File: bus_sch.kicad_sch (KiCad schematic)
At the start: 12 parts, among them J2 Conn_01x01_Female, J3 Conn_01x01_Female, J4 Conn_02x20_Odd_Even, J5 Conn_01x01_Female, J6 Conn_01x01_Female, J7 Conn_01x01_Female, J8 Conn_01x01_Female, J9 Conn_02x10_Odd_Even

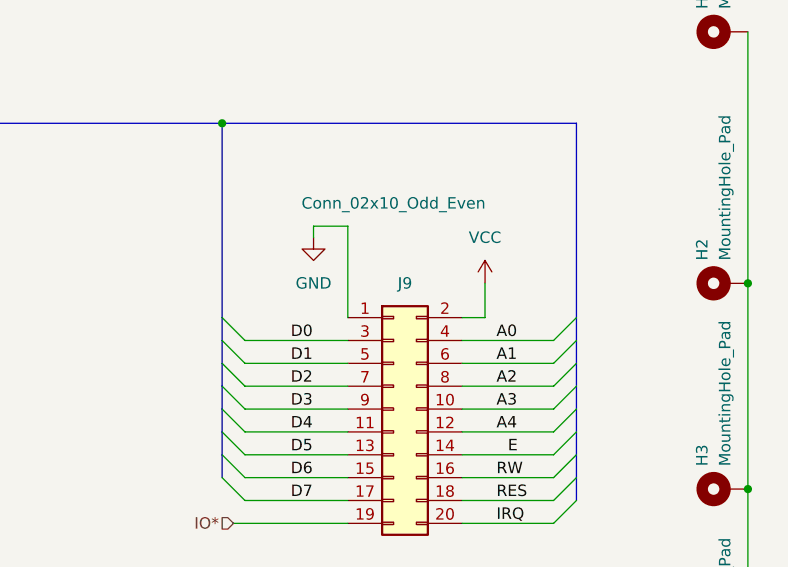
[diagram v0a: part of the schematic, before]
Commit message: Schematic updates
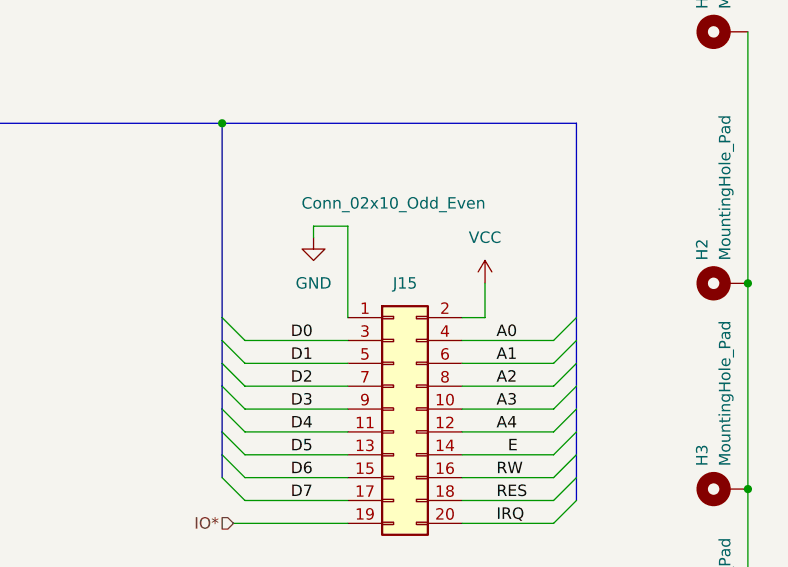
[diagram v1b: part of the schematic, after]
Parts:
- renumbered J9 to J15
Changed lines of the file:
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@@
   (symbol (lib_id "power:VCC") (at 240.03 86.36 0) (unit 1)
     (in_bom yes) (on_board yes) (dnp no)
-    (property "Reference" "#PWR09" (at 240.03 90.17 0)
+    (property "Reference" "#PWR07" (at 240.03 90.17 0)
       (effects (font (size 1.27 1.27)) hide)
     )
@@
   (symbol (lib_id "power:VCC") (at 140.97 87.63 0) (unit 1)
     (in_bom yes) (on_board yes) (dnp no) (fields_autoplaced)
-    (property "Reference" "#PWR06" (at 140.97 91.44 0)
+    (property "Reference" "#PWR04" (at 140.97 91.44 0)
       (effects (font (size 1.27 1.27)) hide)
     )
@@
   (symbol (lib_id "power:GND") (at 124.46 81.28 0) (unit 1)
     (in_bom yes) (on_board yes) (dnp no) (fields_autoplaced)
-    (property "Reference" "#PWR05" (at 124.46 87.63 0)
+    (property "Reference" "#PWR03" (at 124.46 87.63 0)
       (effects (font (size 1.27 1.27)) hide)
     )
@@
   (symbol (lib_id "power:GND") (at 220.98 81.28 0) (unit 1)
     (in_bom yes) (on_board yes) (dnp no) (fields_autoplaced)
-    (property "Reference" "#PWR08" (at 220.98 87.63 0)
+    (property "Reference" "#PWR06" (at 220.98 87.63 0)
       (effects (font (size 1.27 1.27)) hide)
     )
@@
   (symbol (lib_id "Connector_Generic:Conn_02x10_Odd_Even") (at 229.87 100.33 0) (unit 1)
     (in_bom yes) (on_board yes) (dnp no)
-    (property "Reference" "J9" (at 231.14 86.36 0)
+    (property "Reference" "J15" (at 231.14 86.36 0)
       (effects (font (size 1.27 1.27)))
     )
@@
   (symbol (lib_id "power:GND") (at 187.96 144.78 0) (unit 1)
     (in_bom yes) (on_board yes) (dnp no) (fields_autoplaced)
-    (property "Reference" "#PWR07" (at 187.96 151.13 0)
+    (property "Reference" "#PWR05" (at 187.96 151.13 0)
       (effects (font (size 1.27 1.27)) hide)
     )
@@
   (symbol (lib_id "power:VCC") (at 78.74 134.62 0) (unit 1)
     (in_bom yes) (on_board yes) (dnp no)
-    (property "Reference" "#PWR04" (at 78.74 138.43 0)
+    (property "Reference" "#PWR02" (at 78.74 138.43 0)
       (effects (font (size 1.27 1.27)) hide)
     )
@@
   (symbol (lib_id "power:GND") (at 269.24 144.78 0) (unit 1)
     (in_bom yes) (on_board yes) (dnp no) (fields_autoplaced)
-    (property "Reference" "#PWR010" (at 269.24 151.13 0)
-      (effects (font (size 1.27 1.27)) hide)
-    )
+    (property "Reference" "#PWR08" (at 269.24 151.13 0)
+      (effects (font (size 1.27 1.27)) hide)
+    )
